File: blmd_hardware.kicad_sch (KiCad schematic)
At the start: 63 parts, among them J1 MR30PW-F, J2 control, J3 GND, J4 12V, J5 STLink-V3, Q1 RH6G040CH, Q2 RH6G040CH, Q3 RH6G040CH, Q4 RH6G040CH, Q5 RH6G040CH, Q6 RH6G040CH, SW1 reset, SW2 SW_DIP_x02, U1 A4939KLPTR-5-T, U10 STM32G431KBTx, U4 ISO7760FDBQR, U6 ACS711KEXLT-31AB, U7 ACS711KEXLT-31AB, U9 BD41041FJ-C

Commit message: tmp : schemetic is all over except for can
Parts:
- removed D2: blue, LED_SMD:LED_0603_1608Metric_Pad1.05x0.95mm_HandSolder, symbol Device:LED
- removed U1: A4939KLPTR-5-T, Package_SO:HTSSOP-28-1EP_4.4x9.7mm_P0.65mm_EP2.75x6.2mm, symbol blmd:A4939KLPTR-5-T
- removed U10: STM32G431KBTx, Package_QFP:LQFP-32_7x7mm_P0.8mm, symbol MCU_ST_STM32G4:STM32G431KBTx
- removed U4: ISO7760FDBQR, Package_SO:SSOP-16_3.9x4.9mm_P0.635mm, symbol Isolator:Si8660BA-AS1
- added D2, D5, D6, D8: B5819W, Diode_SMD:D_SOD-123, symbol Device:D_Schottky
- added D7: D, symbol Device:D
- added D9: Green, LED_SMD:LED_0603_1608Metric_Pad1.05x0.95mm_HandSolder, symbol Device:LED
- added J6: GH4, symbol Connector:Conn_01x04_Pin
- added L1: 2.2u, symbol Device:L
- added R22: 22k, symbol Device:R
- added R23: 6.8k, symbol Device:R
- added R24: 1k, Resistor_SMD:R_0603_1608Metric_Pad0.98x0.95mm_HandSolder, symbol Device:R
- added U1: ISO6520, Package_SO:SOIC-8_3.9x4.9mm_P1.27mm, symbol Isolator:ISO7320C
- added U2: STSPIN32G4, QFN_IN32G4_STM, symbol blmd:STSPIN32G4
- C12, C2, C3, C4: footprint Capacitor_SMD:C_0603_1608Metric_Pad1.08x0.95mm_HandSolder -> (none)
- C16: value 0.1u -> 10u; footprint Capacitor_SMD:C_0603_1608Metric_Pad1.08x0.95mm_HandSolder -> (none)
- C5: value 0.47u -> 0.1u; footprint Capacitor_SMD:C_0603_1608Metric_Pad1.08x0.95mm_HandSolder -> (none)
- C6: value 1u -> 10u; footprint Capacitor_SMD:C_0603_1608Metric_Pad1.08x0.95mm_HandSolder -> (none)
- C7: value 0.22u -> 22u; footprint Capacitor_SMD:C_0603_1608Metric_Pad1.08x0.95mm_HandSolder -> (none)
- C8: value 10u -> 0.1u; footprint Capacitor_SMD:C_0603_1608Metric_Pad1.08x0.95mm_HandSolder -> (none)
- R11: value 2.2k -> 33k; footprint Resistor_SMD:R_0603_1608Metric_Pad0.98x0.95mm_HandSolder -> (none)
- R12: value 2.2k -> 5k
- R16: footprint Resistor_SMD:R_0603_1608Metric_Pad0.98x0.95mm_HandSolder -> (none)
- R17: value 33k -> 10k; footprint Resistor_SMD:R_0603_1608Metric_Pad0.98x0.95mm_HandSolder -> (none)
- R18: value 33k -> 1.2k; footprint Resistor_SMD:R_0603_1608Metric_Pad0.98x0.95mm_HandSolder -> (none)
- R7: value 15k -> 10k; footprint Resistor_SMD:R_0603_1608Metric_Pad0.98x0.95mm_HandSolder -> (none)
- R8: value 10k -> 33k; footprint Resistor_SMD:R_0603_1608Metric_Pad0.98x0.95mm_HandSolder -> (none)
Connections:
- net +12VA: now also C16.1, R22.1, U2.61 (VM); no longer C7.1
- net +3V3: now also C5.1, C6.1, C8.1, R17.1, D8.1 (K), J6.2 (Pin_2), U1.8 (VCC2), U2.1 (REG3V3/VDD), U2.2 (VBAT), U2.26 (VREF+), U2.27 (VDDA); no longer C12.1, J2.1 (Pin_1)
- net GNDD: now also U1.4 (GND1); no longer C10.2, C11.2, C13.2, C14.2, C15.2, C17.2, C18.2, C19.2, C9.2, D4.1 (K), J5.11 (Pin_11), J5.5 (Pin_5), J5.7 (Pin_7), SW1.1, SW2.3, SW2.4, U6.3 (GND), U7.3 (GND), U9.2 (VSS), U9.8 (STBY)
- net HOA: now also U2.43 (GHS1)
- net HOB: now also U2.40 (GHS2)
- net HOC: now also U2.37 (GHS3)
- net HSA: now also R8.2, U2.42 (OUT1); no longer R16.2
- net HSB: now also C3.2, R11.2, U2.39 (OUT2); no longer C3.1, R17.2
- net HSC: now also C4.2, R16.2, U2.36 (OUT3); no longer C4.1, R18.2
- net ID1: now also U2.57 (PB6)
- net ID2: now also U2.58 (PB7)
- net ID_DISP: now also U2.51 (PA15)
- net LOA: now also U2.29 (GLS1)
- net LOB: now also U2.30 (GLS2)
- net LOC: now also U2.31 (GLS3)
- net NRST: now also U2.8 (PG10/NRST)
- net REF0: now also U2.17 (PA4), U2.18 (PA5), U2.9 (PC0)
- net RXD: now also U2.47 (PA11)
- net SCA: now also U2.23 (PB0)
- net SCC: now also U2.14 (PA1)
- net SPD1: now also U1.2 (INA)
- net SPD2: now also U1.3 (INB)
- net SWCLK: now also U2.50 (PA14)
- net SWDIO: now also U2.49 (PA13)
- net SWO: now also U2.54 (PB3)
- net TXD: now also U2.48 (PA12)
- net at R18.1: now also R17.2, U2.52 (SCREF)
- net at R16.1: now also U2.10 (PC1)
- net GND: now reaches C8.2
- net GND: now also C1.2, C10.2, C11.2, C13.2, C14.2, C15.2, C16.2, C17.2, C18.2, C19.2, C5.2, C6.2, C7.2, C9.2, D1.2 (A), D3.1 (K), D4.1 (K), J3.1 (Pin_1), J3.10 (Pin_10), J3.11 (Pin_11), J3.12 (Pin_12), J3.13 (Pin_13), J3.14 (Pin_14), J3.2 (Pin_2), J3.3 (Pin_3), J3.4 (Pin_4), J3.5 (Pin_5), J3.6 (Pin_6), J3.7 (Pin_7), J3.8 (Pin_8), J3.9 (Pin_9), J5.11 (Pin_11), J5.5 (Pin_5), J5.7 (Pin_7), Q4.1 (S), Q4.2 (S), Q4.3 (S), Q5.1 (S), Q5.2 (S), Q5.3 (S), Q6.1 (S), Q6.2 (S), Q6.3 (S), R18.2, R7.2, SW1.1, SW2.3, SW2.4, U6.3 (GND), U7.3 (GND), U9.2 (VSS), U9.8 (STBY), D7.2 (A), D9.1 (K), J6.4 (Pin_4), R23.2, U1.5 (GND2), U2.32 (PGND), U2.65 (VSS)
- net BOOTA: now reaches C2.2
- net BOOTA: now also D2.1 (K), U2.41 (BOOT1)
- net at R8.1: now also U2.24 (PB1); no longer R7.1
- net at R11.1: now also U2.20 (PA7)
- net USART_TX: now reaches J5.13 (Pin_13)
- net USART_TX: now also U2.45 (PA9)
- net USART_RX: now reaches J5.14 (Pin_14)
- net USART_RX: now also U2.46 (PA10)
- removed net +5V: C16.1, C6.1, R11.2, R12.1, R7.2
- removed net GNDPWR: C1.2, C16.2, C6.2, C7.2, C8.1, D1.2 (A), D3.1 (K), J3.1 (Pin_1), J3.10 (Pin_10), J3.11 (Pin_11), J3.12 (Pin_12), J3.13 (Pin_13), J3.14 (Pin_14), J3.2 (Pin_2), J3.3 (Pin_3), J3.4 (Pin_4), J3.5 (Pin_5), J3.6 (Pin_6), J3.7 (Pin_7), J3.8 (Pin_8), J3.9 (Pin_9), Q4.1 (S), Q4.2 (S), Q4.3 (S), Q5.1 (S), Q5.2 (S), Q5.3 (S), Q6.1 (S), Q6.2 (S), Q6.3 (S), R8.2
- new net: D9.2 (A), R24.2
- new net: D7.1 (K), L1.1, U2.62 (SW)
- new net: U2.33 (NC), U2.34 (NC)
- new net: R7.1, U2.59 (PB8/BOOOT0)
- new net +12V: C7.1, D2.2 (A), D5.2 (A), D6.2 (A), L1.2, R12.1, U2.63 (VCC), U2.64 (REGIN)
- new net +3.3V: C12.1, J2.1 (Pin_1), U1.1 (VCC1)
- new net BOOTB: C3.1, D5.1 (K), U2.38 (BOOT2)
- new net BOOTC: C4.1, D6.1 (K), U2.35 (BOOT3)
- new net COS: J6.3 (Pin_3), U2.12 (PC3)
- new net MON: D8.2 (A), R22.2, R23.1, U2.16 (PA3)
- new net SIN: J6.1 (Pin_1), U2.11 (PC2)
- new net SPD1_O: U1.7 (OUTA), U2.55 (PB4)
- new net SPD2_O: U1.6 (OUTB), U2.56 (PB5)
- new net STATUS: R24.1, U2.53 (PD2)
- no-connect marks 17 -> 28
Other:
- moved on the sheet: C10, C11, C13, C14, C15, C17, C18, C19, C9, D4, J1, J5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

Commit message: tmp : backup commit
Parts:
- U2: footprint QFN_IN32G4_STM -> blmd_hardware:QFN_IN32G4_STM
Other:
- moved on the sheet: R10
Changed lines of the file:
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@@
 	(symbol
 		(lib_id "Device:R")
-		(at 248.92 57.15 180)
+		(at 248.92 57.15 0)
+		(mirror x)
 		(unit 1)
 		(exclude_from_sim no)
@@
 		(dnp no)
 		(property "Reference" "R10"
-			(at 246.38 57.15 90)
+			(at 251.46 57.15 90)
 			(effects
 				(font
@@
 		)
 		(property "Footprint" "Resistor_SMD:R_0603_1608Metric_Pad0.98x0.95mm_HandSolder"
-			(at 250.698 57.15 90)
+			(at 247.142 57.15 90)
 			(effects
 				(font
@@
 			)
 		)
-		(property "Footprint" "QFN_IN32G4_STM"
+		(property "Footprint" "blmd_hardware:QFN_IN32G4_STM"
 			(at 90.17 93.98 0)
 			(effects

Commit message: back up commit
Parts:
- removed D1: TVS, Diode_SMD:D_SOD-523, symbol Device:D_Zener
- removed U9: BD41041FJ-C, Package_SO:SOIC-8_3.9x4.9mm_P1.27mm, symbol Interface_CAN_LIN:MCP2561-E-SN
- added U3: TCAN3414DDFR, Package_TO_SOT_SMD:SOT-23-8, symbol Interface_CAN_LIN:TCAN334
- C1: value 470u -> 330u
- C10: renamed from C16; footprint (none) -> Capacitor_SMD:C_0603_1608Metric_Pad1.08x0.95mm_HandSolder
- C11: renamed from C6; footprint (none) -> Capacitor_SMD:C_0603_1608Metric_Pad1.08x0.95mm_HandSolder
- C12: renamed from C5; footprint (none) -> Capacitor_SMD:C_0603_1608Metric_Pad1.08x0.95mm_HandSolder
- C16: renamed from C12; footprint (none) -> Capacitor_SMD:C_0603_1608Metric_Pad1.08x0.95mm_HandSolder
- C17: renamed from C8; footprint (none) -> Capacitor_SMD:C_0603_1608Metric_Pad1.08x0.95mm_HandSolder
- C2, C3, C4: footprint (none) -> Capacitor_SMD:C_0603_1608Metric_Pad1.08x0.95mm_HandSolder
- C5: renamed from C7; footprint (none) -> Capacitor_SMD:C_0805_2012Metric_Pad1.18x1.45mm_HandSolder
- D1: renamed from D8; value B5819W -> schot; footprint Diode_SMD:D_SOD-123 -> Diode_SMD:D_SOD-323F
- D2: value B5819W -> schot; footprint Diode_SMD:D_SOD-123 -> Diode_SMD:D_SOD-323F
- D3: renamed from D5; value B5819W -> schot; footprint Diode_SMD:D_SOD-123 -> Diode_SMD:D_SOD-323F
- D4: renamed from D6; value B5819W -> schot; footprint Diode_SMD:D_SOD-123 -> Diode_SMD:D_SOD-323F
- D5: renamed from D7; value D -> fast rec; footprint (none) -> Diode_SMD:D_SOD-323F
- J6: footprint (none) -> Connector_JST:JST_GH_SM04B-GHS-TB_1x04-1MP_P1.25mm_Horizontal
- L1: footprint (none) -> Inductor_SMD:L_0603_1608Metric_Pad1.05x0.95mm_HandSolder
- R10: renamed from R8; footprint (none) -> Resistor_SMD:R_0603_1608Metric_Pad0.98x0.95mm_HandSolder
- R11: footprint (none) -> Resistor_SMD:R_0603_1608Metric_Pad0.98x0.95mm_HandSolder
- R12: renamed from R16; footprint (none) -> Resistor_SMD:R_0603_1608Metric_Pad0.98x0.95mm_HandSolder
- R18: renamed from R23; footprint (none) -> Resistor_SMD:R_0603_1608Metric_Pad0.98x0.95mm_HandSolder
- R19: renamed from R22; footprint (none) -> Resistor_SMD:R_0603_1608Metric_Pad0.98x0.95mm_HandSolder
- R20: renamed from R18; footprint (none) -> Resistor_SMD:R_0603_1608Metric_Pad0.98x0.95mm_HandSolder
- R21: renamed from R17; footprint (none) -> Resistor_SMD:R_0603_1608Metric_Pad0.98x0.95mm_HandSolder
- R24: renamed from R7; footprint (none) -> Resistor_SMD:R_0603_1608Metric_Pad0.98x0.95mm_HandSolder
- renumbered C17 to C18, C11 to C19, C18 to C6, C19 to C7, C10 to C8, D3 to D6, D9 to D7, D4 to D8, R14 to R13, R15 to R14, R12 to R15, R24 to R16, R13 to R17, R9 to R22, R10 to R23, R19 to R7, R20 to R8, R21 to R9, U2 to U1, U1 to U2, U6 to U4, U7 to U5
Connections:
- net +3V3: now also C13.1, U3.3 (VCC)
- net +5VD: no longer C13.1
- net CANH: now also U3.7 (CANH)
- net CANL: now also U3.6 (CANL)
- net GND: now also U3.2 (GND), U3.8 (STB)
- net HSA: now also R12.2; no longer R10.2
- net HSC: now also R10.2; no longer R12.2
- net ID1: now also U1.58 (PB7); no longer U1.57 (PB6)
- net ID2: now also U1.57 (PB6); no longer U1.58 (PB7)
- net RXD: now also U3.4 (RXD)
- net TXD: now also U3.1 (TXD)
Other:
- moved on the sheet: C1, C10

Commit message: change : diode from sod-323f to sod-323
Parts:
- D1, D2, D3, D4: value schot -> 1N5819WS; footprint Diode_SMD:D_SOD-323F -> Diode_SMD:D_SOD-323_HandSoldering
- D5: value fast rec -> 1N4148WS; footprint Diode_SMD:D_SOD-323F -> Diode_SMD:D_SOD-323_HandSoldering
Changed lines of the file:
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@@
 			)
 		)
-		(property "Value" "schot"
+		(property "Value" "1N5819WS"
 			(at 161.29 32.0674 90)
 			(effects
@@
 			)
 		)
-		(property "Footprint" "Diode_SMD:D_SOD-323F"
+		(property "Footprint" "Diode_SMD:D_SOD-323_HandSoldering"
 			(at 163.83 30.48 0)
 			(effects
@@
 			)
 		)
-		(property "Value" "schot"
+		(property "Value" "1N5819WS"
 			(at 80.01 74.6126 90)
 			(effects
@@
 			)
 		)
-		(property "Footprint" "Diode_SMD:D_SOD-323F"
+		(property "Footprint" "Diode_SMD:D_SOD-323_HandSoldering"
 			(at 77.47 76.2 0)
 			(effects
@@
 			)
 		)
-		(property "Value" "fast rec"
+		(property "Value" "1N4148WS"
 			(at 167.132 108.204 90)
 			(effects
@@
 			)
 		)
-		(property "Footprint" "Diode_SMD:D_SOD-323F"
+		(property "Footprint" "Diode_SMD:D_SOD-323_HandSoldering"
 			(at 167.64 105.41 0)
 			(effects
@@
 			)
 		)
-		(property "Value" "schot"
+		(property "Value" "1N5819WS"
 			(at 118.11 32.0674 90)
 			(effects
@@
 			)
 		)
-		(property "Footprint" "Diode_SMD:D_SOD-323F"
+		(property "Footprint" "Diode_SMD:D_SOD-323_HandSoldering"
 			(at 120.65 30.48 0)
 			(effects
@@
 			)
 		)
-		(property "Value" "schot"
+		(property "Value" "1N5819WS"
 			(at 74.93 32.0674 90)
 			(effects
@@
 			)
 		)
-		(property "Footprint" "Diode_SMD:D_SOD-323F"
+		(property "Footprint" "Diode_SMD:D_SOD-323_HandSoldering"
 			(at 77.47 30.48 0)
 			(effects

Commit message: complete
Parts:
- R15: value 5k -> 3.3k
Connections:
- net +3V3: now also J6.1 (Pin_1); no longer J6.2 (Pin_2)
- net COS: now also J6.4 (Pin_4); no longer J6.3 (Pin_3)
- net GND: now also J6.3 (Pin_3); no longer J6.4 (Pin_4)
- net SIN: now also J6.2 (Pin_2); no longer J6.1 (Pin_1)
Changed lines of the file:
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@@
 	(wire
 		(pts
-			(xy 33.02 140.97) (xy 40.64 140.97)
+			(xy 167.64 109.22) (xy 175.26 109.22)
 		)
 		(stroke
@@
 	(wire
 		(pts
-			(xy 167.64 109.22) (xy 175.26 109.22)
+			(xy 97.79 36.83) (xy 101.6 36.83)
 		)
 		(stroke
@@
 	(wire
 		(pts
-			(xy 97.79 36.83) (xy 101.6 36.83)
+			(xy 144.78 50.8) (xy 187.96 50.8)
 		)
 		(stroke
@@
 	(wire
 		(pts
-			(xy 144.78 50.8) (xy 187.96 50.8)
+			(xy 229.87 34.29) (xy 229.87 41.91)
 		)
 		(stroke
@@
 	(wire
 		(pts
-			(xy 229.87 34.29) (xy 229.87 41.91)
+			(xy 38.1 80.01) (xy 38.1 82.55)
 		)
 		(stroke
@@
 	(wire
 		(pts
-			(xy 38.1 80.01) (xy 38.1 82.55)
+			(xy 144.78 36.83) (xy 144.78 38.1)
 		)
 		(stroke
@@
 	(wire
 		(pts
-			(xy 144.78 36.83) (xy 144.78 38.1)
+			(xy 33.02 143.51) (xy 40.64 143.51)
 		)
 		(stroke
@@
 	(wire
 		(pts
+			(xy 40.64 143.51) (xy 40.64 146.05)
+		)
+		(stroke
+			(width 0)
+			(type default)
+		)
+	)
+	(wire
+		(pts
 			(xy 144.78 31.75) (xy 144.78 34.29)
 		)
@@
 	(wire
 		(pts
-			(xy 33.02 146.05) (xy 40.64 146.05)
+			(xy 120.65 34.29) (xy 121.92 34.29)
 		)
 		(stroke
@@
 	(wire
 		(pts
-			(xy 120.65 34.29) (xy 121.92 34.29)
+			(xy 229.87 59.69) (xy 229.87 53.34)
 		)
 		(stroke
@@
 	(wire
 		(pts
-			(xy 229.87 59.69) (xy 229.87 53.34)
+			(xy 33.02 138.43) (xy 40.64 138.43)
 		)
 		(stroke
@@
 	(global_label "SIN"
 		(shape output)
-		(at 33.02 138.43 0)
+		(at 33.02 140.97 0)
 		(fields_autoplaced yes)
 		(effects
@@
 		)
 		(property "Intersheetrefs" "${INTERSHEET_REFS}"
-			(at 39.15 138.43 0)
+			(at 39.15 140.97 0)
 			(effects
 				(font
@@
 	(global_label "COS"
 		(shape output)
-		(at 33.02 143.51 0)
+		(at 33.02 146.05 0)
 		(fields_autoplaced yes)
 		(effects
@@
 		)
 		(property "Intersheetrefs" "${INTERSHEET_REFS}"
-			(at 39.8152 143.51 0)
+			(at 39.8152 146.05 0)
 			(effects
 				(font
@@
 	(symbol
 		(lib_id "power:+3V3")
-		(at 40.64 140.97 0)
+		(at 40.64 138.43 0)
 		(unit 1)
 		(exclude_from_sim no)
@@
 		(fields_autoplaced yes)
 		(property "Reference" "#PWR026"
-			(at 40.64 144.78 0)
+			(at 40.64 142.24 0)
 			(effects
 				(font
@@
 		)
 		(property "Value" "+3V3"
-			(at 40.64 135.89 0)
+			(at 40.64 133.35 0)
 			(effects
 				(font
@@
 		)
 		(property "Footprint" ""
-			(at 40.64 140.97 0)
+			(at 40.64 138.43 0)
 			(effects
 				(font
@@
 		)
 		(property "Datasheet" ""
-			(at 40.64 140.97 0)
+			(at 40.64 138.43 0)
 			(effects
 				(font
@@
 		)
 		(property "Description" "Power symbol creates a global label with name \"+3V3\""
-			(at 40.64 140.97 0)
+			(at 40.64 138.43 0)
 			(effects
 				(font
@@
 			)
 		)
-		(property "Value" "5k"
+		(property "Value" "3.3k"
 			(at 53.34 77.4699 0)
 			(effects

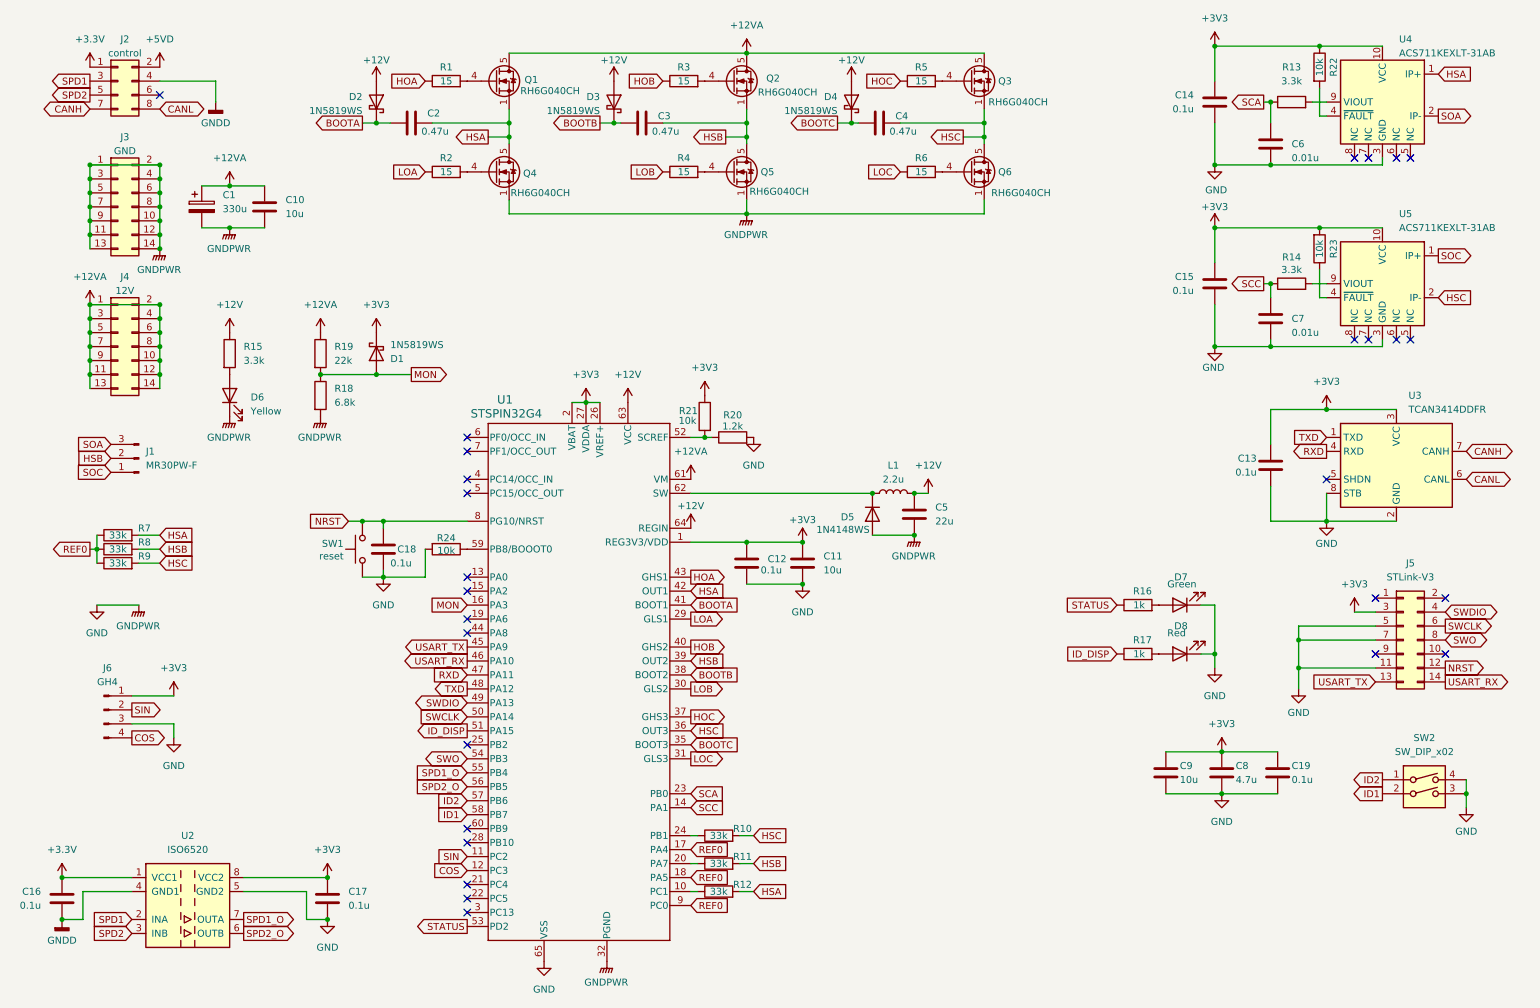
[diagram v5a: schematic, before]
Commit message: fix : emf low path filter
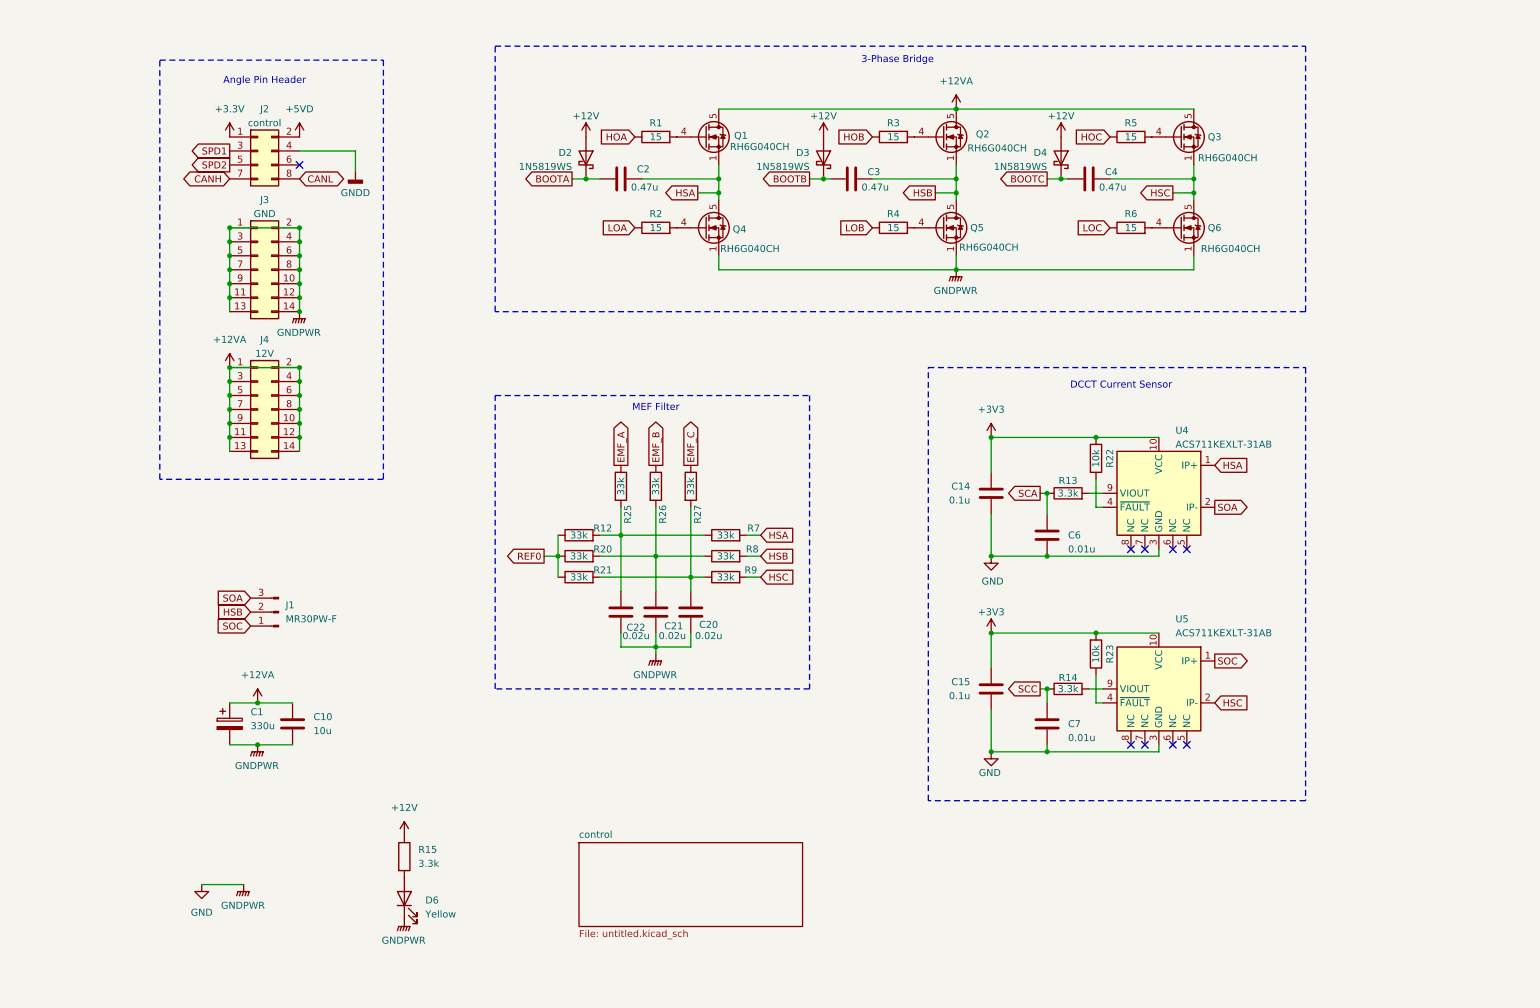
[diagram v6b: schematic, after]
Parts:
- removed C11, C9: 10u, Capacitor_SMD:C_0603_1608Metric_Pad1.08x0.95mm_HandSolder, symbol Device:C
- removed C12, C13, C16, C17, C18, C19: 0.1u, Capacitor_SMD:C_0603_1608Metric_Pad1.08x0.95mm_HandSolder, symbol Device:C
- removed C5: 22u, Capacitor_SMD:C_0805_2012Metric_Pad1.18x1.45mm_HandSolder, symbol Device:C
- removed C8: 4.7u, Capacitor_SMD:C_0603_1608Metric_Pad1.08x0.95mm_HandSolder, symbol Device:C
- removed D1: 1N5819WS, Diode_SMD:D_SOD-323_HandSoldering, symbol Device:D_Schottky
- removed D5: 1N4148WS, Diode_SMD:D_SOD-323_HandSoldering, symbol Device:D
- removed D7: Green, LED_SMD:LED_0603_1608Metric_Pad1.05x0.95mm_HandSolder, symbol Device:LED
- removed D8: Red, LED_SMD:LED_0603_1608Metric_Pad1.05x0.95mm_HandSolder, symbol Device:LED
- removed J5: STLink-V3, blmd_hardware:CONN_3220-14-0300-00_CNC, symbol Connector_Generic:Conn_02x07_Odd_Even
- removed J6: GH4, Connector_JST:JST_GH_SM04B-GHS-TB_1x04-1MP_P1.25mm_Horizontal, symbol Connector:Conn_01x04_Pin
- removed L1: 2.2u, Inductor_SMD:L_0603_1608Metric_Pad1.05x0.95mm_HandSolder, symbol Device:L
- removed R10, R11: 33k, Resistor_SMD:R_0603_1608Metric_Pad0.98x0.95mm_HandSolder, symbol Device:R
- removed R16, R17: 1k, Resistor_SMD:R_0603_1608Metric_Pad0.98x0.95mm_HandSolder, symbol Device:R
- removed R18: 6.8k, Resistor_SMD:R_0603_1608Metric_Pad0.98x0.95mm_HandSolder, symbol Device:R
- removed R19: 22k, Resistor_SMD:R_0603_1608Metric_Pad0.98x0.95mm_HandSolder, symbol Device:R
- removed R24: 10k, Resistor_SMD:R_0603_1608Metric_Pad0.98x0.95mm_HandSolder, symbol Device:R
- removed SW1: reset, blmd_hardware:RESET, symbol Switch:SW_Push
- removed SW2: SW_DIP_x02, Button_Switch_SMD:SW_DIP_SPSTx02_Slide_Copal_CHS-02B_W7.62mm_P1.27mm, symbol Switch:SW_DIP_x02
- removed U1: STSPIN32G4, blmd_hardware:QFN_IN32G4_STM, symbol blmd:STSPIN32G4
- removed U2: ISO6520, Package_SO:SOIC-8_3.9x4.9mm_P1.27mm, symbol Isolator:ISO7320C
- removed U3: TCAN3414DDFR, Package_TO_SOT_SMD:SOT-23-8, symbol Interface_CAN_LIN:TCAN334
- added C20, C21, C22: 0.02u, symbol Device:C
- added R25, R26, R27: 33k, Resistor_SMD:R_0603_1608Metric_Pad0.98x0.95mm_HandSolder, symbol Device:R
- R20: value 1.2k -> 33k
- R21: value 10k -> 33k
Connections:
- net +3V3: no longer R21.1
- net GND: now also C20.2, C21.2, C22.2; no longer R20.2
- net HSA: no longer R12.2
- net REF0: now also R12.1, R20.1, R21.1; no longer R7.1, R8.1, R9.1
- net at R21.2: now also R9.1, C20.1, R27.2; no longer R20.1
- new net: C21.1, R20.2, R26.2, R8.1
- new net: C22.1, R12.2, R25.2, R7.1
- new net EMF_A: R25.1
- new net EMF_B: R26.1
- new net EMF_C: R27.1
- no-connect marks 28 -> 9
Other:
- added sheet control (untitled.kicad_sch)
- note added: "3-Phase Bridge"
- note added: "Angle Pin Header"
- note added: "DCCT Current Sensor"
- note added: "MEF Filter"
- moved on the sheet: C14, C15, C2, C3, C4, C6, C7, D2, D3, D4, D6, J1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
